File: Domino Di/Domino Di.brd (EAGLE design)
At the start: 71.1 x 33 mm, 51 parts, among them J1 LiPo Battery, J2 MH28-1, J3 MH28-1, M1 DOMINO, SW1 IT-1210, U1 AMS1117-3.3, U2 MCP73831T-2ACI/OT

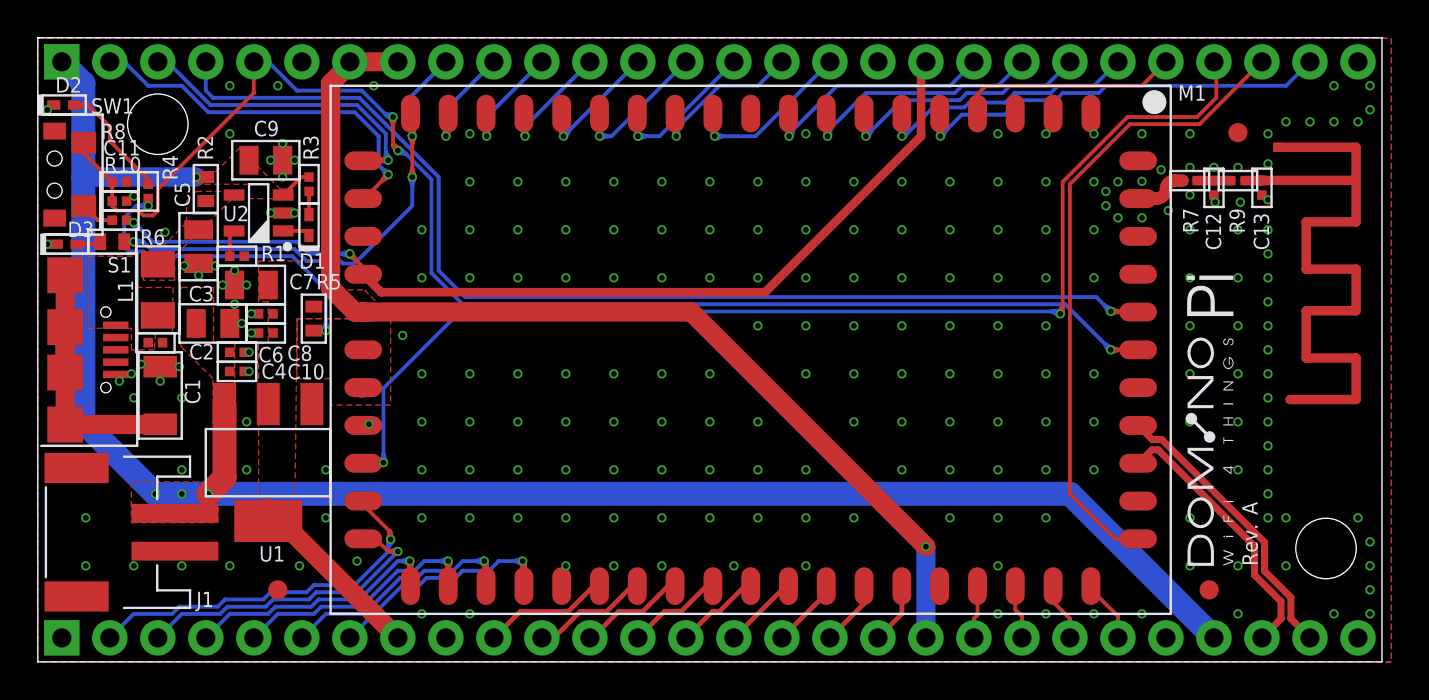
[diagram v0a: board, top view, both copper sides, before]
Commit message: Domino Di Rev. A: added slider switch
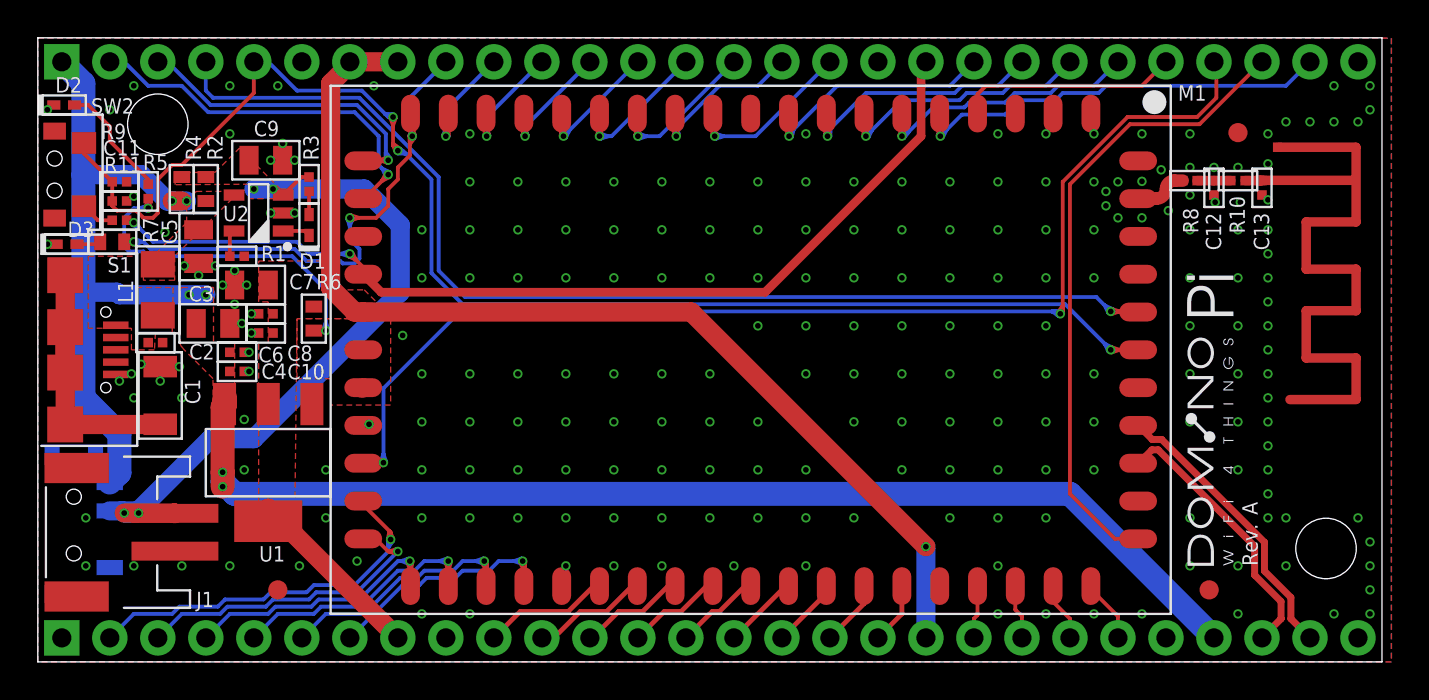
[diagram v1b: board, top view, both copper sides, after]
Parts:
- added R11: 1k, Domino:R0402
- added SW2: IT-1210, Domino:IT-1210
- R10: value 1k -> 0R
- R4: value 270R -> 0R; device Domino:R0402 -> Domino:R0603
- R5: value 0R -> 270R; device Domino:R0603 -> Domino:R0402
- R6: value 270R -> 0R
- R7: value 0R -> 270R; device Domino:R0402 -> Domino:R0603
- R8: value 10k -> 0R
- R9: value 0R -> 10k
- SW1: value IT-1210 -> MK-12C01; device Domino:IT-1210 -> Domino:MK-12C01
- moved R10 59.2 mm to (63.5, 25.5)
- moved R9 59.2 mm to (4.32, 25.4), turned to 180 degrees
- moved R7 57.1 mm to (3.94, 22.2)
- moved R8 56.6 mm to (61.0, 25.5), turned to 0 degrees
- moved SW1 18.6 mm to (1.91, 7.24), flipped to the bottom
- moved R6 11.4 mm to (14.6, 18.2), turned to 270 degrees
- moved R5 11.0 mm to (5.84, 24.9)
- moved R4 1.78 mm to (7.62, 25.0)
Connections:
- new net VBAT: C9.1, J1.2, R2.2, R3.2, R4.1, SW1.2, U2.3
- net +2V5: now also R11.2; no longer R10.2
- net +3.3VD_IN: now also R6.2; no longer R4.2
- net +3V3: now also R6.1; no longer R5.1
- net +5V: now also R4.2, SW1.3; no longer C9.1, J1.2, R2.2, R3.2, U2.3
- net ANT0: now also R8.1; no longer R7.1
- net ANT0_50R: now also R10.2; no longer R9.2
- net ANT0_EXT: now also R10.1, R8.2; no longer R7.2, R9.1
- net BLUE_LED: now also R7.1; no longer R6.1
- net GND: now also R9.1, SW1.4, SW1.5, SW1.6, SW1.7, SW2.SH$1, SW2.SH$2; no longer R8.1, SW1.SH$1, SW1.SH$2
- net JUMPSTART: now also R11.1, SW2.1; no longer R10.1, SW1.1
- net LED0: now also R7.2; no longer R6.2
- net N$1: now also R5.1; no longer R4.1
- net UART_RTS: now also R9.2, SW2.2; no longer R8.2, SW1.2
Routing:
- net VBAT: track 0.00 -> 37.7 mm, vias 0 -> 4
- net LED0: track 34.6 -> 35.8 mm
- net +3.3VD_IN: track 19.6 -> 20.8 mm
- net +5V: track 97.6 -> 98.0 mm, vias 4 -> 6
- added copper zone on layer 1, net VBAT

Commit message: Domino Di Rev. B: removed battery charger as too complex
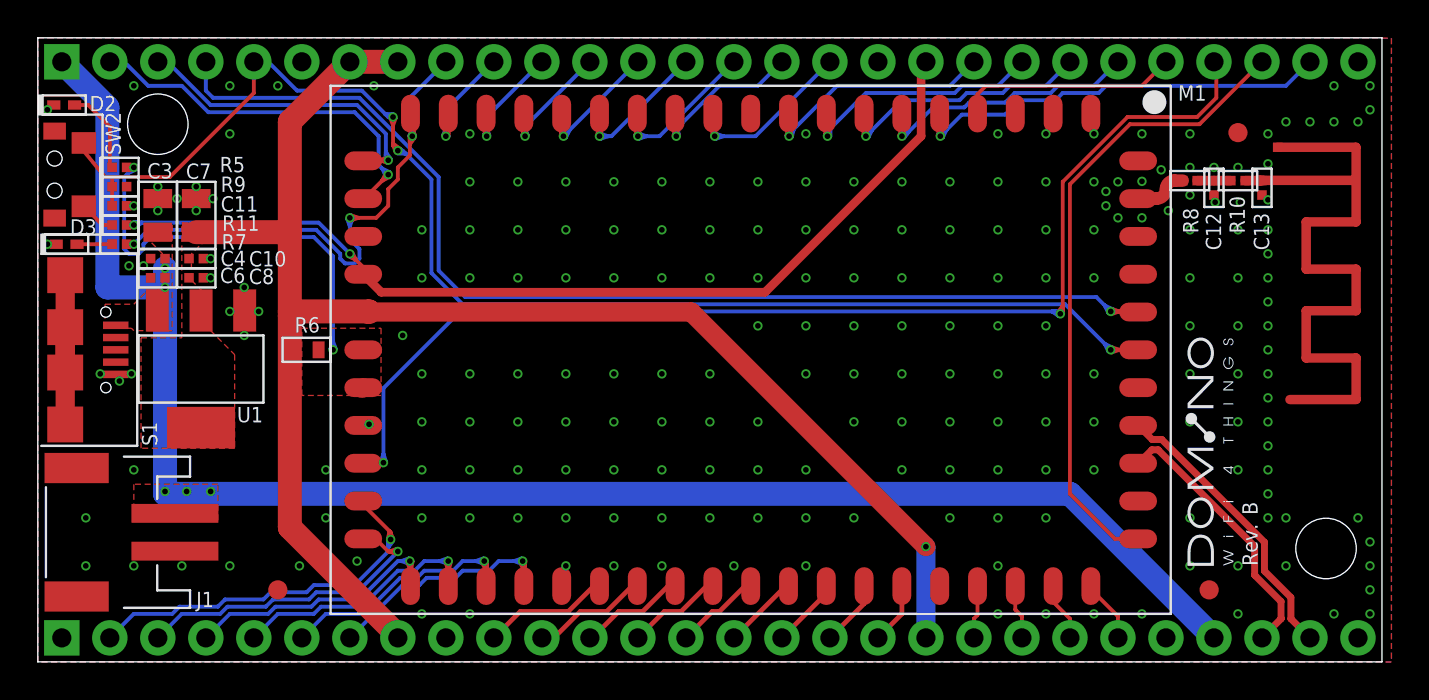
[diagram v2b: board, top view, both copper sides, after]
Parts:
- removed C1: 1n, Domino:C1206
- removed C2: 10n, Domino:C0402
- removed C5, C9: 4u7, Domino:C0805
- removed D1: GREEN, Domino:LED0402
- removed L1: BLM31PG601SN1L, Domino:FB1206
- removed R1: 2k, Domino:R0402
- removed R2, R4: 0R, Domino:R0603
- removed R3: 330R, Domino:R0402
- removed SW1: MK-12C01, Domino:MK-12C01
- removed U2: MCP73831T-2ACI/OT, Domino:SOT23-5
- R7: device Domino:R0603 -> Domino:R0402
- U$6, U$8: device Domino:DOMINO_PI_LOGO_SMALL -> Domino:DOMINO_LOGO_SMALL
- W1: value DOMINO_PI_LOGO -> DOMINO_LOGO; device Domino:DOMINO_PI_LOGO -> Domino:DOMINO_LOGO
- moved C4 7.29 mm to (6.35, 21.3), turned to 180 degrees
- moved C3 6.42 mm to (6.35, 23.6), turned to 90 degrees
- moved U1 6.10 mm to (8.64, 15.5)
- moved C6 5.75 mm to (6.35, 20.3), turned to 180 degrees
- moved C10 5.39 mm to (8.38, 21.3), turned to 0 degrees
- moved C7 4.70 mm to (8.38, 23.6), turned to 90 degrees
- moved C8 4.15 mm to (8.38, 20.3), turned to 0 degrees
- moved R5 1.98 mm to (4.32, 26.2), turned to 0 degrees
- moved R6 1.69 mm to (14.2, 16.5), turned to 0 degrees
- moved R7 0.40 mm to (4.32, 22.1)
- moved C11 0.25 mm to (4.32, 24.1)
- moved R11 0.25 mm to (4.32, 23.1)
- moved R9 0.25 mm to (4.32, 25.1)
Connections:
- removed net N$2: D1.1, U2.1
- removed net N$3: D1.2, R3.1
- removed net N$5: R1.2, U2.5
- removed net PE: C1.1, S1.SH$1, S1.SH$2, S1.SH$3, S1.SH$4
- removed net VBAT: C9.1, J1.2, R2.2, R3.2, R4.1, SW1.2, U2.3
- removed net VBUS: C2.1, L1.2, S1.1
- removed net VUSB: C5.1, L1.1, R2.1, U2.4
- net +5V: now also J1.2, S1.1; no longer R4.2, SW1.3
- net GND: now also S1.SH$1, S1.SH$2, S1.SH$3, S1.SH$4; no longer C1.2, C2.2, C5.2, C9.2, R1.1, SW1.4, SW1.5, SW1.6, SW1.7, U2.2
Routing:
- net VBAT: track 37.7 -> 0.00 mm, vias 4 -> 0
- net +3V3: track 67.3 -> 88.3 mm
- net PE: track 15.5 -> 0.00 mm
- net +5V: track 98.0 -> 86.6 mm, vias 6 -> 5
- net GND: track 0.00 -> 10.5 mm, vias 232 -> 222
- net +3.3VD_IN: track 20.8 -> 24.3 mm
- net UART_RTS: track 80.9 -> 78.9 mm
- net LED0: track 35.8 -> 34.1 mm
- net N$1: track 6.23 -> 4.55 mm
- net N$2: track 1.46 -> 0.00 mm
- net N$5: track 1.43 -> 0.00 mm
- net N$3: track 1.23 -> 0.00 mm
- net +2V5: track 54.7 -> 53.6 mm
- net BLUE_LED: track 1.28 -> 1.86 mm
- removed copper zone on layer 1, net VBAT
- removed copper zone on layer 1, net VBUS
- removed copper zone on layer 1, net VUSB
